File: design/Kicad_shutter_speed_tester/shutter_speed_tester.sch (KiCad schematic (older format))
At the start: 17 parts, among them J1 Light Sensor, J2 Light source LED, J3 LCD, J4 Power, Q1 PN2222A, SW1 Reset switch

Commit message: adding routing
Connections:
- net GND: now also J4.1 (Pin_1); no longer J4.2 (Pin_2)
- net at A1.30 (VIN): now also J4.2 (Pin_2); no longer J4.1 (Pin_1)
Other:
- moved on the sheet: J4
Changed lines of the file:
@@
 F 3 "~" H 8000 4050 50  0001 C CNN
 	1    8000 4050
-	1    0    0    -1
+	1    0    0    1
 $EndComp
 $Comp
@@
 Wire Wire Line
 	5550 1650 5550 2400
-Wire Wire Line
-	7800 4150 7800 5150
 Wire Wire Line
 	5750 5150 5750 4400
@@
 Connection ~ 6150 1650
 Wire Wire Line
-	7800 1650 7800 4050
+	7800 1650 7800 3950
 Wire Wire Line
 	7800 1650 6150 1650
@@
 	-1   0    0    -1
 $EndComp
+Wire Wire Line
+	7800 4050 7800 5150
 $EndSCHEMATC

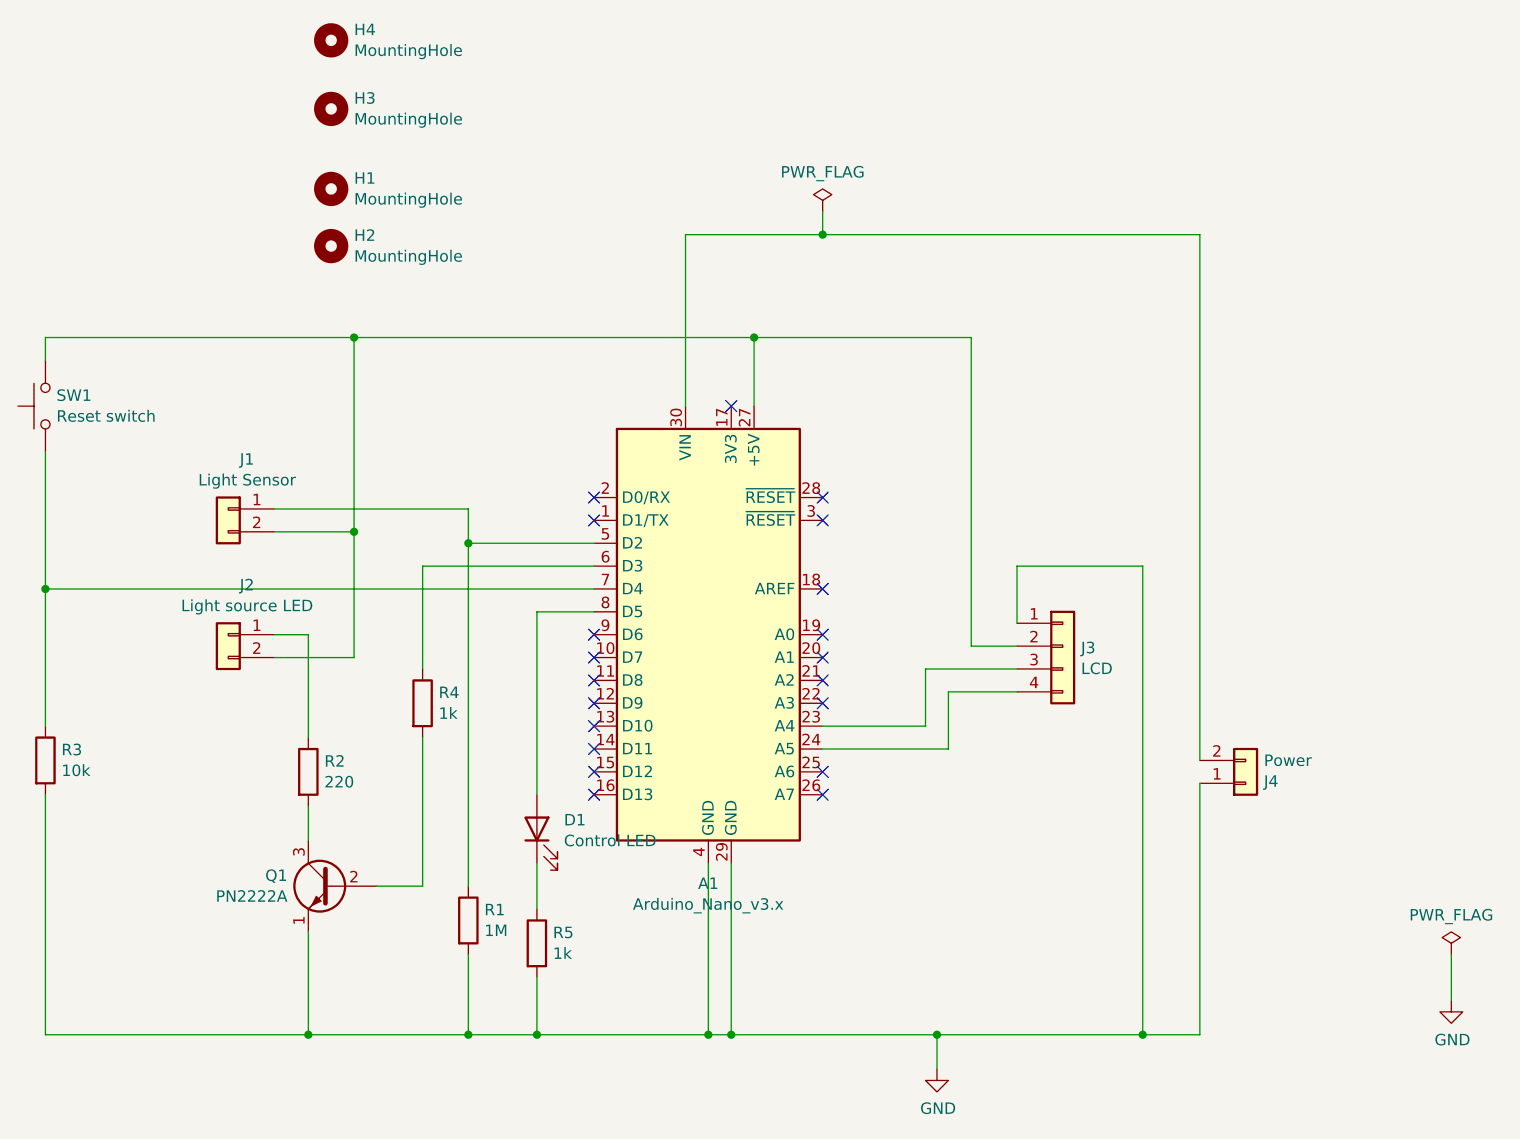
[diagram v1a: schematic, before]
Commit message: reorganize pcb with USB port on top
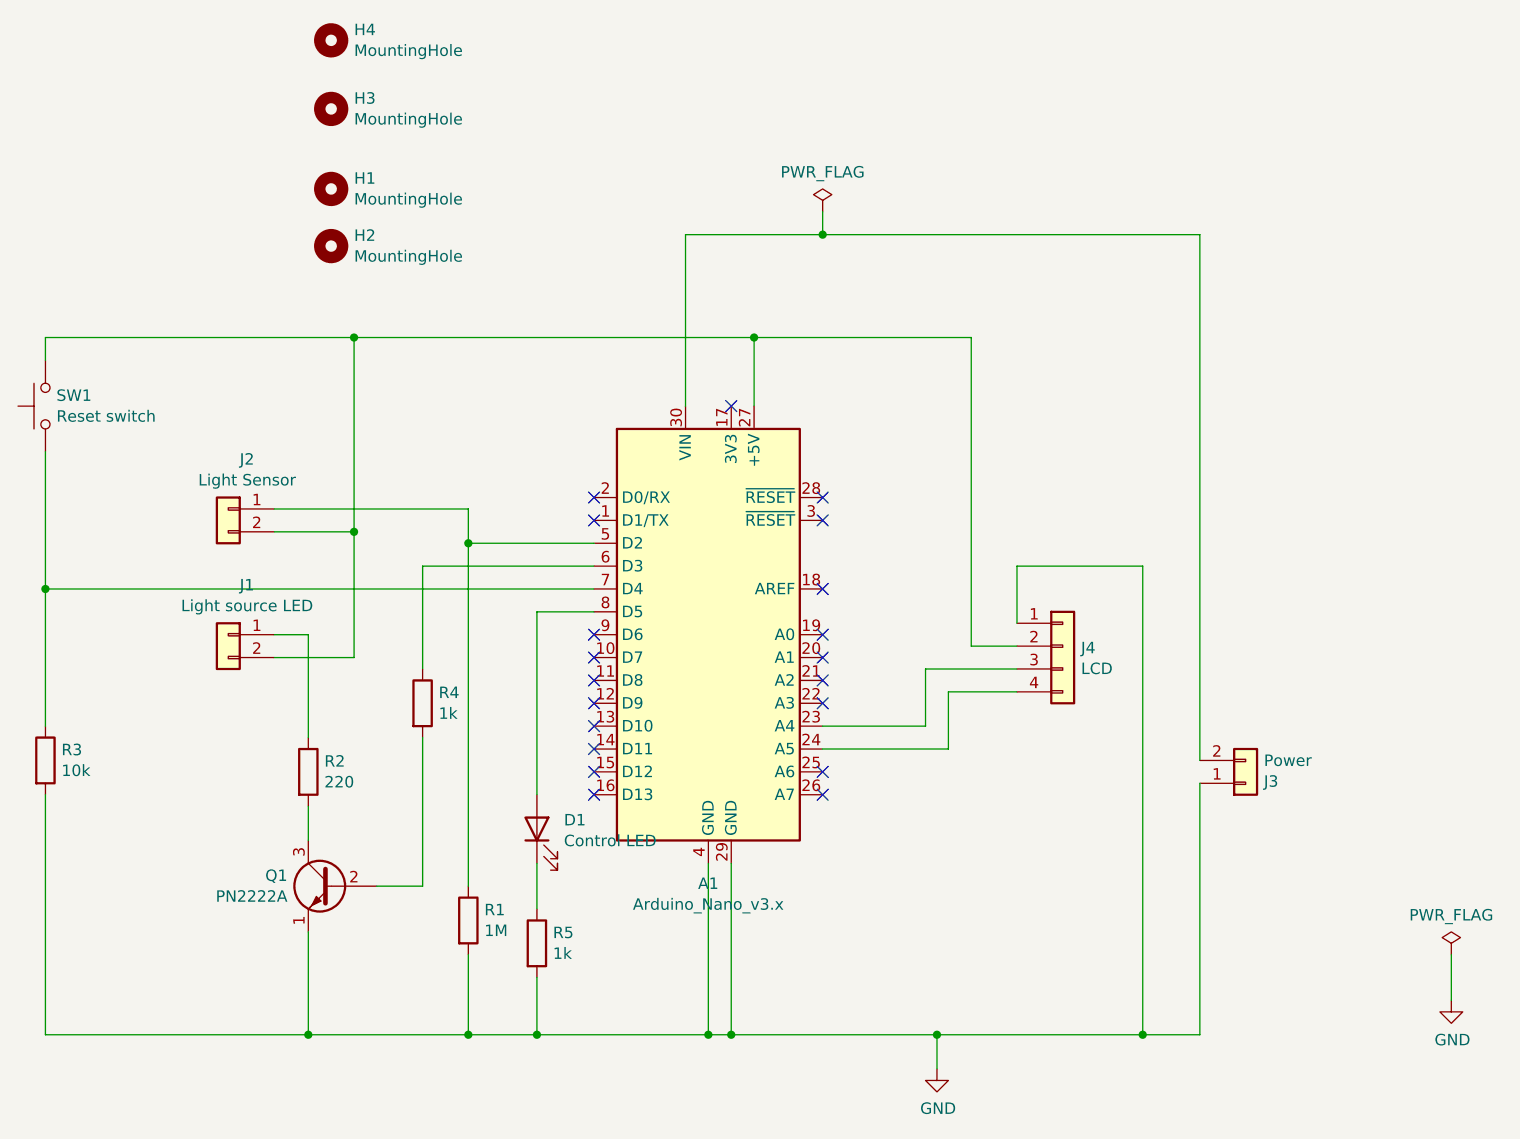
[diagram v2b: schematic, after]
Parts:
- renumbered J2 to J1, J1 to J2, J4 to J3, J3 to J4
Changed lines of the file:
@@
 $EndComp
 $Comp
-L Connector_Generic:Conn_01x02 J4
+L Connector_Generic:Conn_01x02 J3
 U 1 1 619F5383
 P 8000 4050
-F 0 "J4" H 8080 4042 50  0000 L CNN
+F 0 "J3" H 8080 4042 50  0000 L CNN
 F 1 "Power" H 8080 3951 50  0000 L CNN
 F 2 "Connector_Molex:Molex_KK-254_AE-6410-02A_1x02_P2.54mm_Vertical" H 8000 4050 50  0001 C CNN
@@
 $EndComp
 $Comp
-L Connector_Generic:Conn_01x04 J3
+L Connector_Generic:Conn_01x04 J4
 U 1 1 61A01F58
 P 7200 3450
-F 0 "J3" H 7280 3442 50  0000 L CNN
+F 0 "J4" H 7280 3442 50  0000 L CNN
 F 1 "LCD" H 7280 3351 50  0000 L CNN
 F 2 "Connector_Molex:Molex_KK-254_AE-6410-04A_1x04_P2.54mm_Vertical" H 7200 3450 50  0001 C CNN
@@
 	8900 4800 8900 5000
 $Comp
-L Connector_Generic:Conn_01x02 J2
+L Connector_Generic:Conn_01x02 J1
 U 1 1 61A421B1
 P 3550 3400
-F 0 "J2" H 3468 3617 50  0000 C CNN
+F 0 "J1" H 3468 3617 50  0000 C CNN
 F 1 "Light source LED" H 3468 3526 50  0000 C CNN
 F 2 "Connector_Molex:Molex_KK-254_AE-6410-02A_1x02_P2.54mm_Vertical" H 3550 3400 50  0001 C CNN
@@
 $EndComp
 $Comp
-L Connector_Generic:Conn_01x02 J1
+L Connector_Generic:Conn_01x02 J2
 U 1 1 61A42B79
 P 3550 2850
-F 0 "J1" H 3468 3067 50  0000 C CNN
+F 0 "J2" H 3468 3067 50  0000 C CNN
 F 1 "Light Sensor" H 3468 2976 50  0000 C CNN
 F 2 "Connector_Molex:Molex_KK-254_AE-6410-02A_1x02_P2.54mm_Vertical" H 3550 2850 50  0001 C CNN

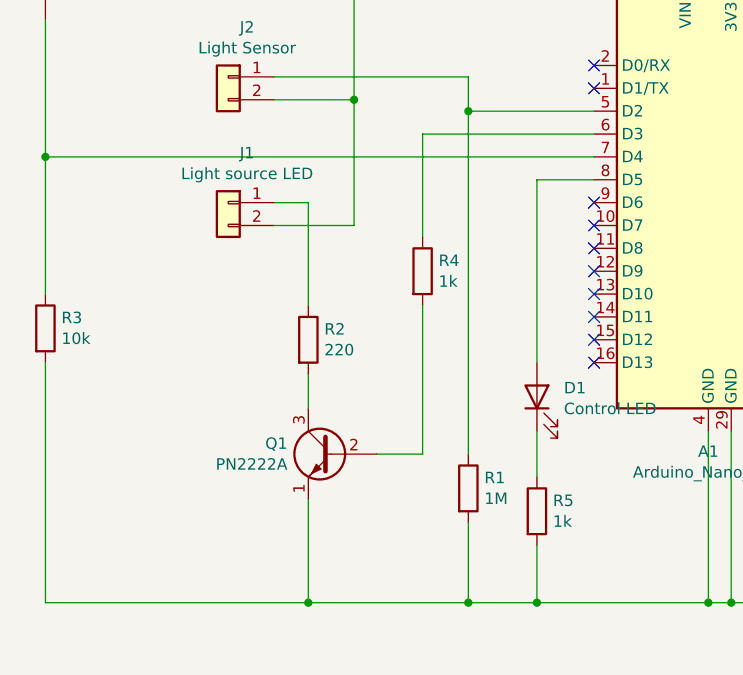
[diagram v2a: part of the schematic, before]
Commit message: Changes on PCB, fixes #2, fixes #3, fixes #4
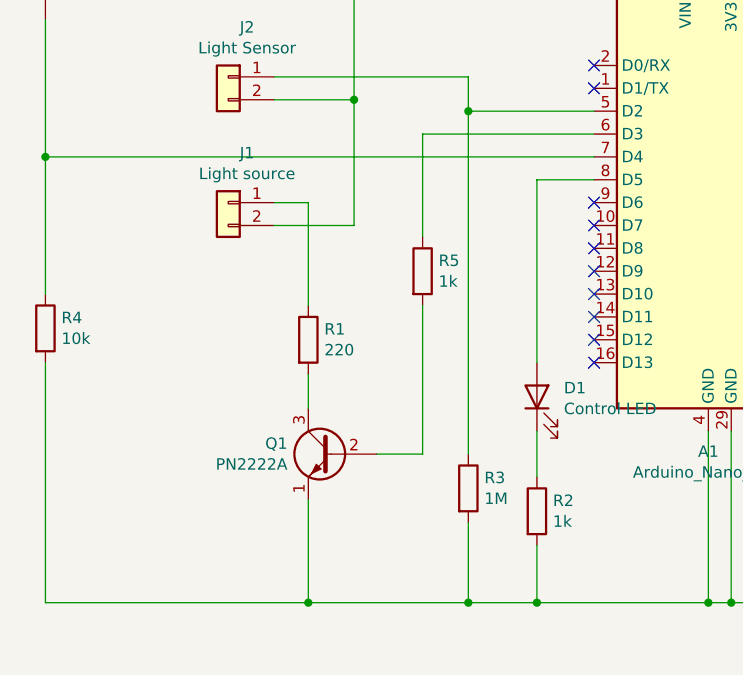
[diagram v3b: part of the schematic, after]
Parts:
- J1: value Light source LED -> Light source
- Q1: footprint Package_TO_SOT_THT:TO-92_Inline -> Package_TO_SOT_THT:TO-92_Inline_Wide
- R1: renamed from R2; footprint Resistor_THT:R_Axial_DIN0204_L3.6mm_D1.6mm_P5.08mm_Horizontal -> Resistor_THT:R_Axial_DIN0207_L6.3mm_D2.5mm_P7.62mm_Horizontal
- R2: renamed from R5; footprint Resistor_THT:R_Axial_DIN0204_L3.6mm_D1.6mm_P5.08mm_Horizontal -> Resistor_THT:R_Axial_DIN0207_L6.3mm_D2.5mm_P7.62mm_Horizontal
- R3: renamed from R1; footprint Resistor_THT:R_Axial_DIN0204_L3.6mm_D1.6mm_P5.08mm_Horizontal -> Resistor_THT:R_Axial_DIN0207_L6.3mm_D2.5mm_P7.62mm_Horizontal
- R4: renamed from R3; footprint Resistor_THT:R_Axial_DIN0204_L3.6mm_D1.6mm_P5.08mm_Horizontal -> Resistor_THT:R_Axial_DIN0207_L6.3mm_D2.5mm_P7.62mm_Horizontal
- R5: renamed from R4; footprint Resistor_THT:R_Axial_DIN0204_L3.6mm_D1.6mm_P5.08mm_Horizontal -> Resistor_THT:R_Axial_DIN0207_L6.3mm_D2.5mm_P7.62mm_Horizontal
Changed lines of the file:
@@
 Connection ~ 5750 5150
 $Comp
-L Device:R R1
+L Device:R R3
 U 1 1 619FF074
 P 4600 4650
-F 0 "R1" H 4670 4696 50  0000 L CNN
+F 0 "R3" H 4670 4696 50  0000 L CNN
 F 1 "1M" H 4670 4605 50  0000 L CNN
-F 2 "Resistor_THT:R_Axial_DIN0204_L3.6mm_D1.6mm_P5.08mm_Horizontal" V 4530 4650 50  0001 C CNN
+F 2 "Resistor_THT:R_Axial_DIN0207_L6.3mm_D2.5mm_P7.62mm_Horizontal" V 4530 4650 50  0001 C CNN
 F 3 "~" H 4600 4650 50  0001 C CNN
 	1    4600 4650
@@
 F 0 "Q1" H 4191 4546 50  0000 L CNN
 F 1 "PN2222A" H 4191 4455 50  0000 L CNN
-F 2 "Package_TO_SOT_THT:TO-92_Inline" H 4200 4425 50  0001 L CIN
+F 2 "Package_TO_SOT_THT:TO-92_Inline_Wide" H 4200 4425 50  0001 L CIN
 F 3 "https://www.onsemi.com/pub/Collateral/PN2222-D.PDF" H 4000 4500 50  0001 L CNN
 	1    4000 4500
@@
 $EndComp
 $Comp
-L Device:R R4
+L Device:R R5
 U 1 1 61A0A5DF
 P 4400 3700
-F 0 "R4" H 4470 3746 50  0000 L CNN
+F 0 "R5" H 4470 3746 50  0000 L CNN
 F 1 "1k" H 4470 3655 50  0000 L CNN
-F 2 "Resistor_THT:R_Axial_DIN0204_L3.6mm_D1.6mm_P5.08mm_Horizontal" V 4330 3700 50  0001 C CNN
+F 2 "Resistor_THT:R_Axial_DIN0207_L6.3mm_D2.5mm_P7.62mm_Horizontal" V 4330 3700 50  0001 C CNN
 F 3 "~" H 4400 3700 50  0001 C CNN
 	1    4400 3700
@@
 Connection ~ 4100 2950
 $Comp
-L Device:R R2
+L Device:R R1
 U 1 1 61A0D8F9
 P 3900 4000
-F 0 "R2" H 3970 4046 50  0000 L CNN
+F 0 "R1" H 3970 4046 50  0000 L CNN
 F 1 "220" H 3970 3955 50  0000 L CNN
-F 2 "Resistor_THT:R_Axial_DIN0204_L3.6mm_D1.6mm_P5.08mm_Horizontal" V 3830 4000 50  0001 C CNN
+F 2 "Resistor_THT:R_Axial_DIN0207_L6.3mm_D2.5mm_P7.62mm_Horizontal" V 3830 4000 50  0001 C CNN
 F 3 "~" H 3900 4000 50  0001 C CNN
 	1    3900 4000
@@
 	2750 3200 2750 2600
 $Comp
-L Device:R R3
+L Device:R R4
 U 1 1 61A1C5D0
 P 2750 3950
-F 0 "R3" H 2820 3996 50  0000 L CNN
+F 0 "R4" H 2820 3996 50  0000 L CNN
 F 1 "10k" H 2820 3905 50  0000 L CNN
-F 2 "Resistor_THT:R_Axial_DIN0204_L3.6mm_D1.6mm_P5.08mm_Horizontal" V 2680 3950 50  0001 C CNN
+F 2 "Resistor_THT:R_Axial_DIN0207_L6.3mm_D2.5mm_P7.62mm_Horizontal" V 2680 3950 50  0001 C CNN
 F 3 "~" H 2750 3950 50  0001 C CNN
 	1    2750 3950
@@
 $EndComp
 $Comp
-L Device:R R5
+L Device:R R2
 U 1 1 61A22621
 P 4900 4750
-F 0 "R5" H 4970 4796 50  0000 L CNN
+F 0 "R2" H 4970 4796 50  0000 L CNN
 F 1 "1k" H 4970 4705 50  0000 L CNN
-F 2 "Resistor_THT:R_Axial_DIN0204_L3.6mm_D1.6mm_P5.08mm_Horizontal" V 4830 4750 50  0001 C CNN
+F 2 "Resistor_THT:R_Axial_DIN0207_L6.3mm_D2.5mm_P7.62mm_Horizontal" V 4830 4750 50  0001 C CNN
 F 3 "~" H 4900 4750 50  0001 C CNN
 	1    4900 4750
@@
 P 3550 3400
 F 0 "J1" H 3468 3617 50  0000 C CNN
-F 1 "Light source LED" H 3468 3526 50  0000 C CNN
+F 1 "Light source" H 3468 3526 50  0000 C CNN
 F 2 "Connector_Molex:Molex_KK-254_AE-6410-02A_1x02_P2.54mm_Vertical" H 3550 3400 50  0001 C CNN
 F 3 "~" H 3550 3400 50  0001 C CNN

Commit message: Set control LED size to 5mm
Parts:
- D1: footprint LED_THT:LED_D3.0mm -> LED_THT:LED_D5.0mm
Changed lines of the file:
@@
 F 0 "D1" V 4939 4132 50  0000 R CNN
 F 1 "Control LED" V 4848 4132 50  0000 R CNN
-F 2 "LED_THT:LED_D3.0mm" H 4900 4250 50  0001 C CNN
+F 2 "LED_THT:LED_D5.0mm" H 4900 4250 50  0001 C CNN
 F 3 "~" H 4900 4250 50  0001 C CNN
 	1    4900 4250
